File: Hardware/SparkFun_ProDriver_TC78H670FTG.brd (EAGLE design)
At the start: 50.8 x 57.1 mm, 137 parts, among them J2 LATCH, J3 PTH, J4 LATCH, J5 LATCH, J6 PTH, J7 LATCH, J8 PTH, U1 TC78H670FTG, U2 LM1117

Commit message: Added new jeep pro driver logo to bottom silk
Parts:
- added U$41: PRODRIVER_LOGO, TC78H670FTG:PRODRIVER_LOGO
- added U$71: (no value), SparkFun-Aesthetics:OSHW-LOGO-S
- LOGO5: device SparkFun-Aesthetics:SFE_LOGO_NAME_FLAME_.1 -> SparkFun-Aesthetics:SFE_LOGO_FLAME_.1
- moved U$84 39.6 mm to (11.6, 32.6), turned to 90 degrees
- moved U$85 38.9 mm to (13.6, 29.0), turned to 90 degrees
- moved U$86 34.7 mm to (15.8, 32.5), turned to 90 degrees
- moved LOGO5 6.56 mm to (46.4, 16.9), turned to 90 degrees
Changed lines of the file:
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@@
 <?xml version="1.0" encoding="utf-8"?>
 <!DOCTYPE eagle SYSTEM "eagle.dtd">
-<eagle version="9.5.2">
+<eagle version="9.6.2">
 <drawing>
 <settings>
@@
 <setting verticaltext="up"/>
 </settings>
-<grid distance="0.05" unitdist="inch" unit="inch" style="lines" multiple="1" display="yes" altdistance="0.0001" altunitdist="inch" altunit="inch"/>
+<grid distance="0.05" unitdist="inch" unit="inch" style="lines" multiple="1" display="yes" altdistance="0.005" altunitdist="inch" altunit="inch"/>
 <layers>
 <layer number="1" name="Top" color="4" fill="1" visible="yes" active="yes"/>
@@
 <element name="U$83" library="output" package="PWR0" value="" x="0.533396875" y="6.162040625" smashed="yes"/>
 <element name="LOGO3" library="SparkFun-Aesthetics" package="ORDERING_INSTRUCTIONS" value="SPECIAL_INSTRUCTIONS-ORDERING" x="-22.86" y="-17.78" smashed="yes"/>
-<element name="U$84" library="output" package="TC78H670FTG0" value="" x="46.9315875" y="14.655796875" smashed="yes" rot="MR0"/>
-<element name="U$85" library="output" package="STEPPER_MOTOR_DRIVER0" value="" x="50.45965" y="16.51253125" smashed="yes" rot="MR0"/>
-<element name="U$86" library="output" package="PRODRIVER0" value="" x="47.492925" y="18.440396875" smashed="yes" rot="MR0"/>
-<element name="LOGO5" library="SparkFun-Aesthetics" package="SFE_LOGO_NAME_FLAME_.1" value="SFE_LOGO_NAME_FLAME.1_INCH" x="41.135303125" y="20.8508625" smashed="yes" rot="MR0"/>
+<element name="U$84" library="output" package="TC78H670FTG0" value="" x="11.607796875" y="32.5704125" smashed="yes" rot="MR90"/>
+<element name="U$85" library="output" package="STEPPER_MOTOR_DRIVER0" value="" x="13.59153125" y="29.04235" smashed="yes" rot="MR90"/>
+<element name="U$86" library="output" package="PRODRIVER0" value="" x="15.773396875" y="32.517075" smashed="yes" rot="MR90"/>
+<element name="LOGO5" library="SparkFun-Aesthetics" package="SFE_LOGO_FLAME_.1" value="SFE_LOGO_NAME_FLAME.1_INCH" x="46.3778625" y="16.903696875" smashed="yes" rot="MR90"/>
 <element name="U$87" library="output" package="##STBY##0" value="" x="6.276340625" y="42.1005" smashed="yes" rot="MR0"/>
 <element name="U$53" library="output" package="##STBY##1" value="" x="16.51508125" y="55.514240625" smashed="yes" rot="R270"/>
@@
 <element name="U$45" library="output" package="#_POWER_INPUT_3#3#16V_#0" value="" x="32.7533" y="17.592040625" smashed="yes"/>
 <element name="LOGO6" library="SparkFun-Aesthetics" package="SFE_LOGO_FLAME_.1" value="SFE_LOGO_FLAME.1_INCH" x="33.99028125" y="23.860753125" smashed="yes"/>
+<element name="U$41" library="TC78H670FTG" package="PRODRIVER_LOGO" value="PRODRIVER_LOGO" x="39.243" y="20.701" smashed="yes" rot="MR90"/>
+<element name="U$71" library="SparkFun-Aesthetics" package="OSHW-LOGO-S" value="" x="26.67" y="2.54" smashed="yes" rot="MR0"/>
 </elements>
 <signals>

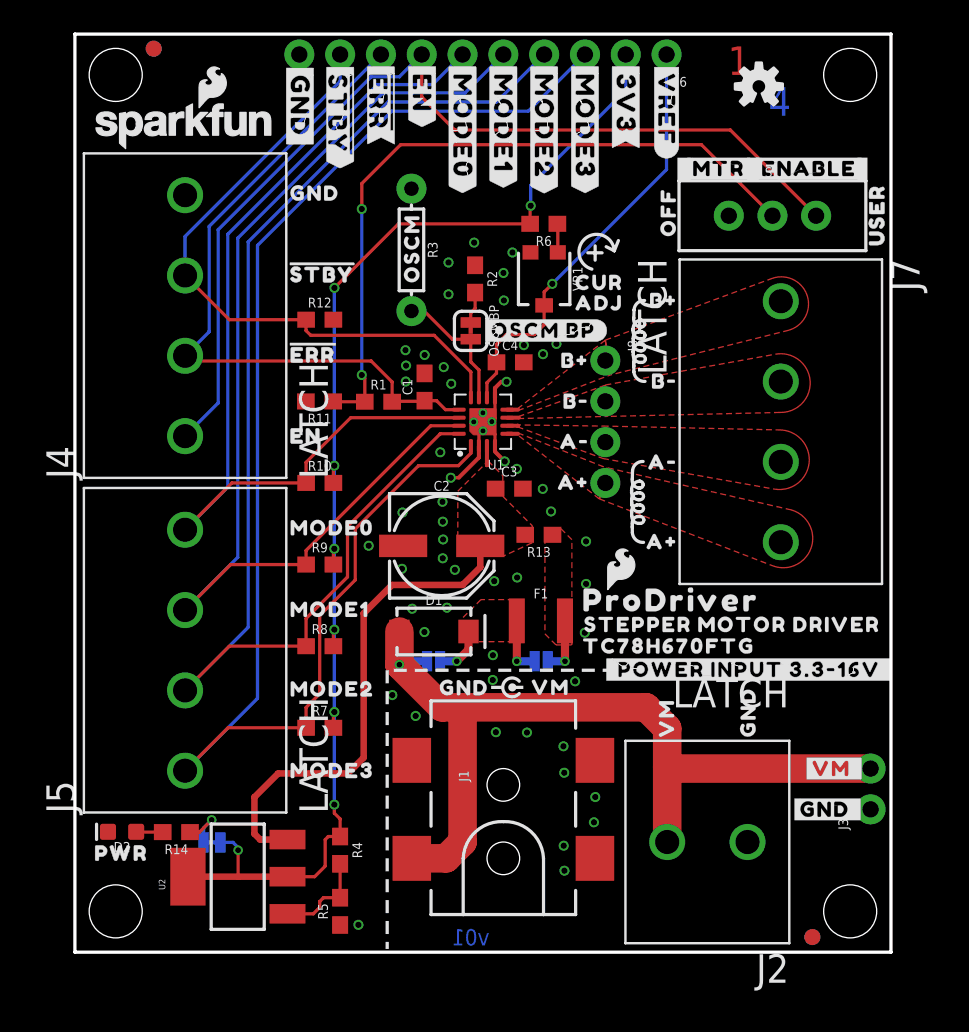
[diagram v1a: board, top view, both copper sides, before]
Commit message: Rotated bottom silk labels to match product name/logo
also updated version number to v10 in brd bottom copper and sch
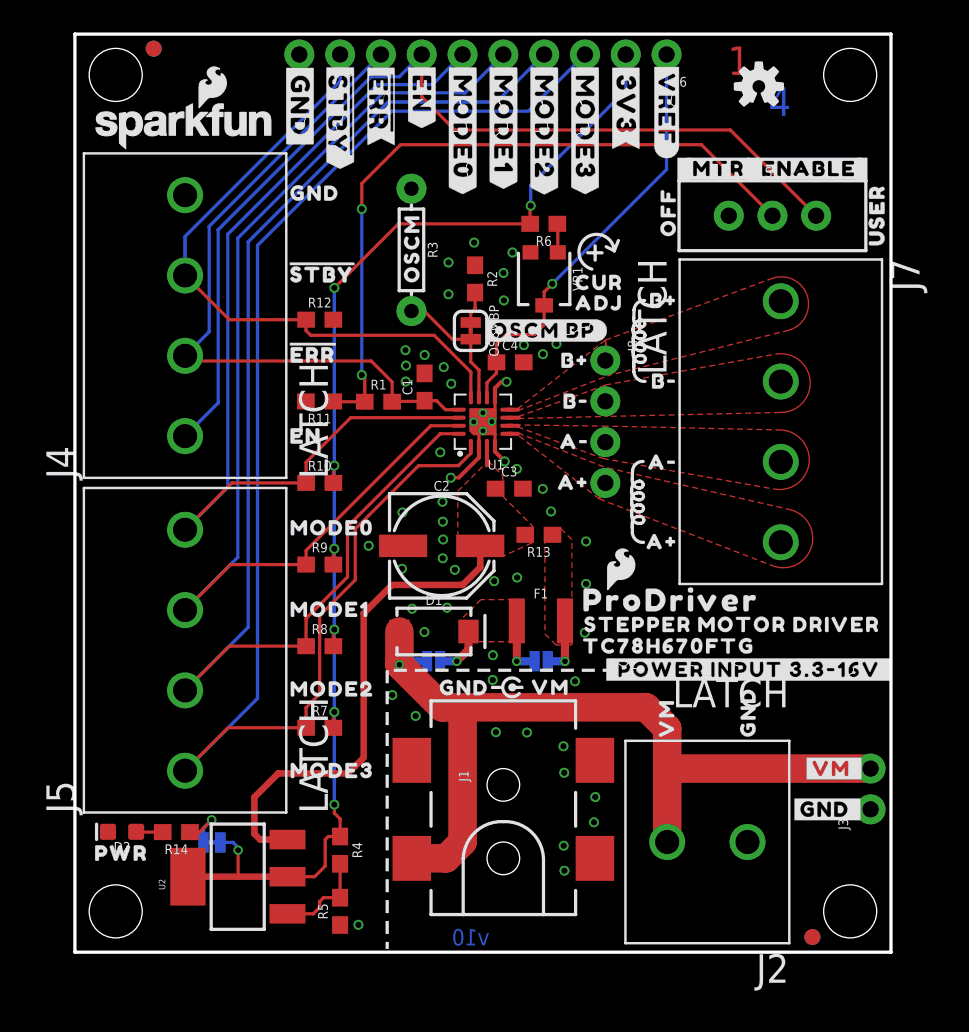
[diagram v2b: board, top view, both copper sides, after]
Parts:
- removed U$36: (no value), output:##ERR##6
- removed U$39: (no value), output:#LED#0
- removed U$76: (no value), output:#MODE0#4
- removed U$77: (no value), output:#MODE1#4
- removed U$78: (no value), output:#MODE2#4
- removed U$79: (no value), output:#MODE3#4
- removed U$81: (no value), output:#VREF#0
- removed U$88: (no value), output:##STBY##1
- added U$74: (no value), output:#MODE0#1
- added U$90: (no value), output:#MODE1#1
- added U$91: (no value), output:#MODE2#2
- added U$92: (no value), output:#MODE3#3
- added U$93: (no value), output:#3V3#4
- added U$94: (no value), output:#EN#5
- added U$95: (no value), output:##ERR##6
- added U$96: (no value), output:#GND#8
- U$35: device output:#3V3#4 -> output2:##ERR##5
- U$38: device output:#D1_BP#0 -> output:#LED#10
- U$54: device output:##ERR##6 -> output:##STBY##7
- U$64: device output:#PTC_BP#0 -> output:#D1_BP#10
- U$70: device output:#GND#5 -> output:#PTC_BP#9
- U$75: device output:#EN#4 -> output2:#3V3#4
- U$80: device output:#3V3#4 -> output:#VREF#4
- moved U$70 38.2 mm to (29.0, 17.5), turned to 90 degrees
- moved U$38 17.9 mm to (8.53, 6.07), turned to 90 degrees
- moved U$35 15.2 mm to (19.1, 55.5)
- moved U$75 12.7 mm to (34.3, 55.5), flipped to the top
- moved U$64 6.74 mm to (22.3, 17.4), turned to 90 degrees
- moved U$54 2.54 mm to (16.5, 55.6), turned to 90 degrees
- moved U$80 2.54 mm to (36.8, 55.6), turned to 90 degrees
- moved U$73 0.12 mm to (41.9, 2.82), turned to 90 degrees
- moved U$72 0.07 mm to (36.9, 2.91), turned to 90 degrees
- moved U$13 0.07 mm to (21.6, 55.5)
- moved U$33 0.07 mm to (24.1, 55.5)
- moved U$46 0.07 mm to (26.7, 55.5)
- moved U$47 0.07 mm to (29.2, 55.5)
- moved U$48 0.07 mm to (31.8, 55.5)
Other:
- board text added: "v10"
- board text removed: "v01"

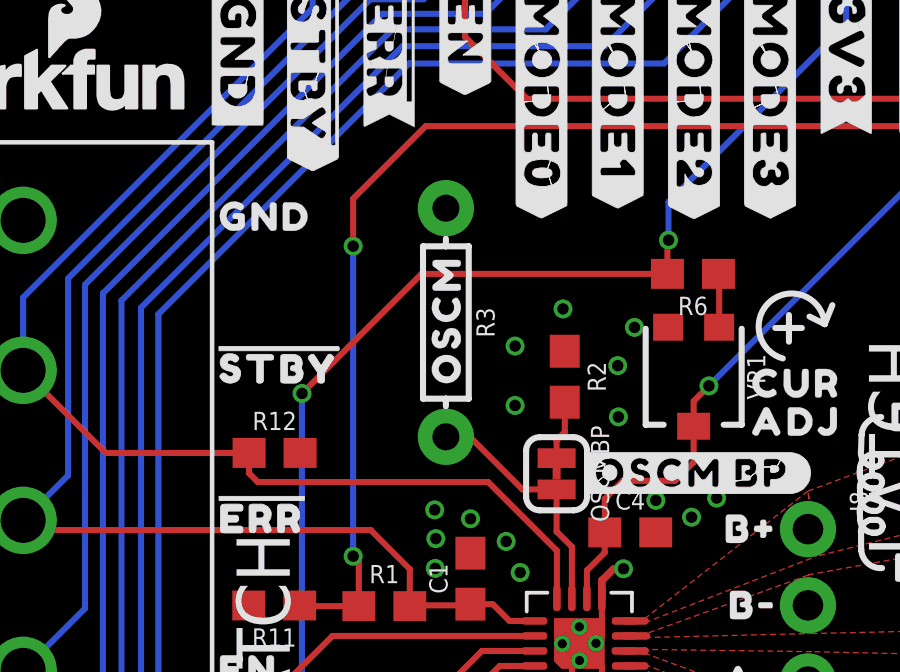
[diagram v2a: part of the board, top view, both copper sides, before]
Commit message: Post design reveiew (REDs)
-Moved R3 (OSCM) away from exposed bottom copper (for the optional heat sink). This is nice to add a little extra clarance in case you want to use a larger heatsink.
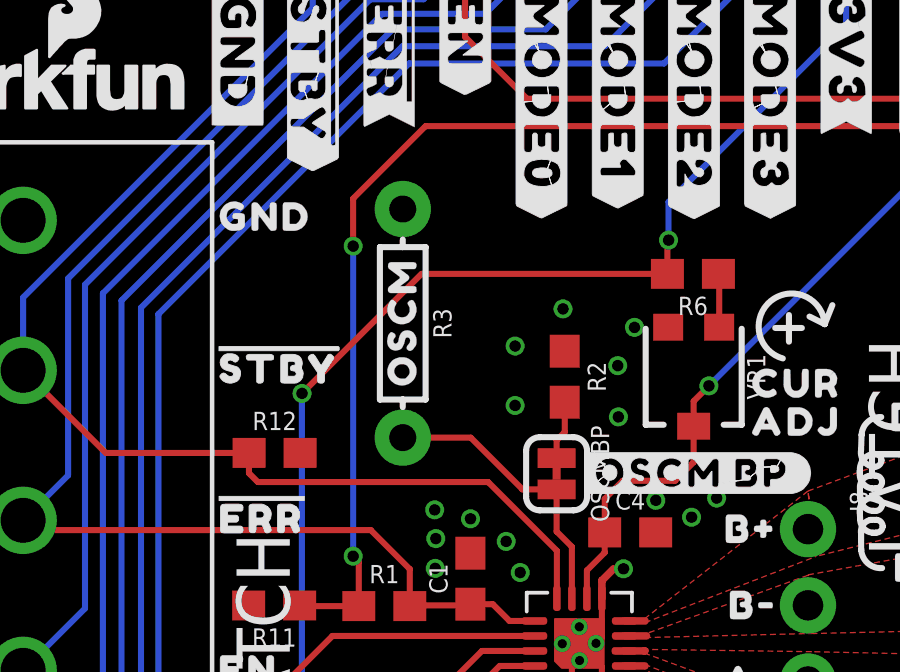
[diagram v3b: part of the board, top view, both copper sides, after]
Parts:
- moved U$18 1.48 mm to (19.5, 40.9)
- moved R3 1.44 mm to (19.5, 43.7)
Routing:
- net OSCM: track 8.26 -> 9.68 mm
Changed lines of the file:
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@@
 <attribute name="VALUE" x="24.150321875" y="41.91" size="0.6096" layer="27" font="vector" ratio="20" rot="R270" align="top-center"/>
 </element>
-<element name="R3" library="SparkFun-Resistors" package="AXIAL-0.3" value="DNP" x="20.94991875" y="43.71848125" smashed="yes" rot="R270">
-<attribute name="NAME" x="21.96591875" y="43.71848125" size="0.6096" layer="25" font="vector" ratio="20" rot="R270" align="bottom-center"/>
-<attribute name="PROD_ID" value=" " x="20.94991875" y="43.71848125" size="1.778" layer="27" font="vector" ratio="15" rot="R270" display="off"/>
-<attribute name="VALUE" x="19.93391875" y="43.71848125" size="0.6096" layer="27" font="vector" ratio="20" rot="R270" align="top-center"/>
+<element name="R3" library="SparkFun-Resistors" package="AXIAL-0.3" value="DNP" x="19.512278125" y="43.690540625" smashed="yes" rot="R270">
+<attribute name="NAME" x="20.528278125" y="43.690540625" size="0.6096" layer="25" font="vector" ratio="20" rot="R270" align="bottom-center"/>
+<attribute name="PROD_ID" value=" " x="19.512278125" y="43.690540625" size="1.778" layer="27" font="vector" ratio="15" rot="R270" display="off"/>
+<attribute name="VALUE" x="18.496278125" y="43.690540625" size="0.6096" layer="27" font="vector" ratio="20" rot="R270" align="top-center"/>
 </element>
 <element name="OSCMBP" library="SparkFun-Jumpers" package="SMT-JUMPER_2_NC_TRACE_SILK" package3d_urn="urn:adsk.eagle:package:39281/1" value="" x="24.6405375" y="38.676578125" smashed="yes" rot="R270">
@@
 <element name="U$12" library="output" package="GND6" value="" x="41.91" y="12.7" smashed="yes" rot="R90"/>
 <element name="U$17" library="output" package="OFF0" value="" x="36.9417625" y="43.863259375" smashed="yes" rot="R90"/>
-<element name="U$18" library="output" package="OSCM0" value="" x="20.980396875" y="40.98544375" smashed="yes" rot="R90"/>
+<element name="U$18" library="output" package="OSCM0" value="" x="19.499575" y="40.90924375" smashed="yes" rot="R90"/>
 <element name="U$10" library="output" package="CUR0" value="" x="30.4546" y="41.6814" smashed="yes"/>
 <element name="U$20" library="output" package="ADJ0" value="" x="30.4546" y="40.4114" smashed="yes"/>
@@
 <wire x1="25.15" y1="36.2418" x2="24.6405375" y2="36.7512625" width="0.2032" layer="1"/>
 <wire x1="24.6405375" y1="38.155878125" x2="23.50008125" y2="38.155878125" width="0.2032" layer="1"/>
-<wire x1="21.747478125" y1="39.90848125" x2="20.94991875" y2="39.90848125" width="0.2032" layer="1"/>
-<wire x1="23.50008125" y1="38.155878125" x2="21.747478125" y2="39.90848125" width="0.2032" layer="1"/>
+<wire x1="21.77541875" y1="39.880540625" x2="19.512278125" y2="39.880540625" width="0.2032" layer="1"/>
+<wire x1="23.50008125" y1="38.155878125" x2="21.77541875" y2="39.880540625" width="0.2032" layer="1"/>
 </signal>
 <signal name="!STBY">

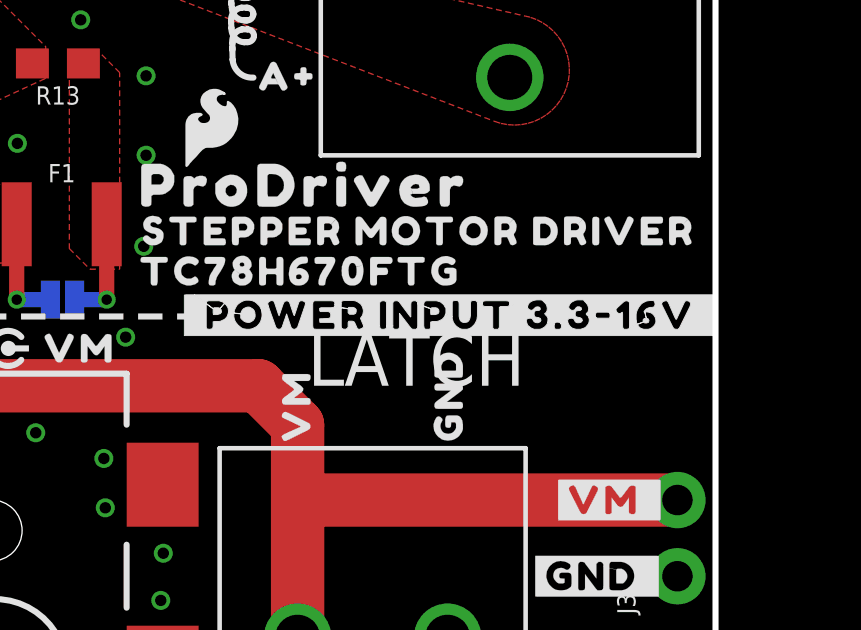
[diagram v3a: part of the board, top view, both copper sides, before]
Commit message: Corrected input voltage range to 3.6-16V on sch and brd
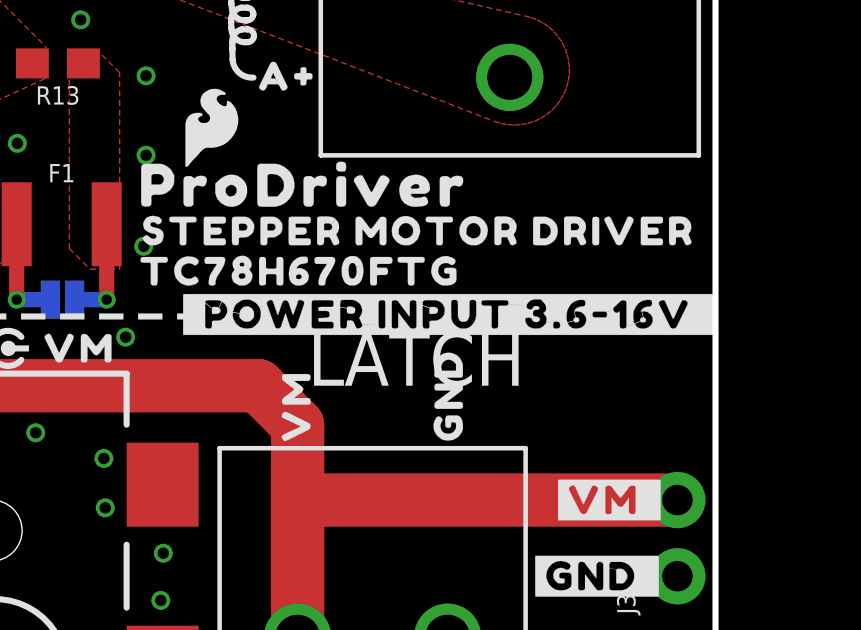
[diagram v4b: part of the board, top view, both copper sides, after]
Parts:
- removed U$45: (no value), output:#_POWER_INPUT_3#3#16V_#0
- added U$36: (no value), output:#_POWER_INPUT_3#6#16V_#0
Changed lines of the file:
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@@
 <layer number="28" name="bValues" color="7" fill="1" visible="no" active="yes"/>
 <layer number="29" name="tStop" color="30" fill="5" visible="no" active="yes"/>
-<layer number="30" name="bStop" color="7" fill="6" visible="no" active="yes"/>
+<layer number="30" name="bStop" color="7" fill="6" visible="yes" active="yes"/>
 <layer number="31" name="tCream" color="7" fill="4" visible="no" active="yes"/>
 <layer number="32" name="bCream" color="7" fill="5" visible="no" active="yes"/>
@@
 <element name="U$7" library="output" package="USER0" value="" x="49.9237" y="43.2816" smashed="yes" rot="R90"/>
 <element name="U$16" library="output" package="#OSCM_BP#0" value="" x="25.229821875" y="38.6994375" smashed="yes"/>
-<element name="U$45" library="output" package="#_POWER_INPUT_3#3#16V_#0" value="" x="32.7533" y="17.592040625" smashed="yes"/>
 <element name="LOGO6" library="SparkFun-Aesthetics" package="SFE_LOGO_FLAME_.1" value="SFE_LOGO_FLAME.1_INCH" x="33.99028125" y="23.860753125" smashed="yes"/>
 <element name="U$41" library="TC78H670FTG" package="PRODRIVER_LOGO" value="PRODRIVER_LOGO" x="39.243" y="20.701" smashed="yes" rot="MR90"/>
@@
 <element name="U$75" library="output2" package="#3V3#4" value="" x="34.29761875" y="55.48121875" smashed="yes" rot="R270"/>
 <element name="U$35" library="output2" package="##ERR##5" value="" x="19.05761875" y="55.48121875" smashed="yes" rot="R270"/>
+<element name="U$36" library="output" package="#_POWER_INPUT_3#6#16V_#0" value="" x="32.7152" y="17.6149" smashed="yes"/>
 </elements>
 <signals>
